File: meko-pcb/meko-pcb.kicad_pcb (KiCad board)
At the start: 4 copper layers, 37 x 69 mm, 131 parts, among them IC1 AS5600-ASOM, IC2 TPS7A2033PDBVR, IC3 TPS7A2033PDBVR, IC4 ES9218PQ, IC5 TPS7A2018PDBVR, IC6 TPS7A2033PDBVR, J1 GDEY0154D67, J2 MEM2090-00-145-00-A, J3 USB_C_Receptacle_USB2.0_16P, J4 SJ2-35954B-SMT-TR, M1 HD-EMB1204-SM, Q3 SS8050, Q4 Si1308EDL, SW1 SW_Push, SW2 SW_Push, SW3 SW_Push, SW4 SW_Push, SW5 SW_Push, SW6 SW_Push, SW7 SW_Push, U1 nRF5340-QKxx, U2 nPM1300-QEXX, Y1 ECS-2520SMV-500-GP-TR, Y2 32MHz, Y4 32.768 kHz

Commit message: many small fixes
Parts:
- removed the C24 at (40.1, 30.6)
- removed the C25 at (26.2, 33.8)
- removed the C26 at (26.2, 35.8)
- removed the C43 at (89.0, 33.3)
- removed the C45 at (94.3, 38.4)
- removed the C49 at (93.9, 40.7)
- removed the C50 at (83.9, 37.5)
- removed the C51 at (90.6, 32.9)
- removed the C52 at (90.6, 33.9)
- removed the C53 at (84.8, 36.5)
- removed the C54 at (96.4, 36.7)
- removed the C55 at (86.3, 37.3)
- removed the D2 at (74.8, 45.3)
- removed the IC5 at (22.1, 37.2)
- removed IC6: TPS7A2033PDBVR, TPS7A2018PDBVR:SOT95P280X145-5N
- removed the JP5 at (26.9, 31.0)
- removed the JP7 at (96.2, 33.3)
- removed JP9: SolderJumper_2_Open, Jumper:SolderJumper-2_P1.3mm_Open_RoundedPad1.0x1.5mm
- removed R27, R33, R35: 10k, Resistor_SMD:R_0402_1005Metric
- removed R28, R29: 47k, Resistor_SMD:R_0402_1005Metric
- removed TP13, TP16: TestPoint, TestPoint:TestPoint_Pad_D1.0mm
- removed the Y1 at (85.6, 41.4)
- added AE1: Antenna_Chip, Diode_SMD:D_1206_3216Metric, F.Cu at (127.5, 89.4)
- added C10: 100nF, Capacitor_SMD:C_0603_1608Metric, F.Cu at (25.6, 43.3)
- added C16: 10uF, Capacitor_SMD:C_0603_1608Metric, F.Cu at (22.8, 51.2)
- added C21: 10uF, Capacitor_SMD:C_0603_1608Metric, F.Cu at (22.8, 53.1)
- added C23: 10uF, Capacitor_SMD:C_0603_1608Metric, F.Cu at (22.8, 57.1)
- added C30: 1uF, Capacitor_SMD:C_0603_1608Metric, F.Cu at (22.8, 47.2)
- added C35: 1uF, Capacitor_SMD:C_0603_1608Metric, F.Cu at (22.8, 45.3)
- added C37: 1uF, Capacitor_SMD:C_0603_1608Metric, F.Cu at (31.4, 49.2)
- added C39: 1uF, Capacitor_SMD:C_0603_1608Metric, F.Cu at (31.4, 47.2)
- added C58: 2.2uF, Capacitor_SMD:C_0603_1608Metric, F.Cu at (28.5, 47.2)
- added C59: 1uF, Capacitor_SMD:C_0603_1608Metric, F.Cu at (28.5, 49.2)
- added C60: 2.2nF, Capacitor_SMD:C_0603_1608Metric, F.Cu at (28.5, 53.1)
- added C65: 4.7uF, Capacitor_SMD:C_0603_1608Metric, F.Cu at (25.6, 55.1)
- added C66: 4.7uF, Capacitor_SMD:C_0603_1608Metric, F.Cu at (25.6, 57.1)
- added C67: 12pF, Capacitor_SMD:C_0603_1608Metric, F.Cu at (22.8, 49.2)
- added C68: 12pF, Capacitor_SMD:C_0603_1608Metric, F.Cu at (31.4, 51.2)
- added C69: 1uF, Capacitor_SMD:C_0603_1608Metric, F.Cu at (25.6, 49.2)
- added C70: 4.7uF, Capacitor_SMD:C_0603_1608Metric, F.Cu at (28.5, 43.3)
- added C71: 4.7uF, Capacitor_SMD:C_0603_1608Metric, F.Cu at (28.5, 45.3)
- added C72: 1uF, Capacitor_SMD:C_0603_1608Metric, F.Cu at (25.6, 51.2)
- added C74: 4.7uF, Capacitor_SMD:C_0603_1608Metric, F.Cu at (25.6, 53.1)
- added D10: D_TVS, Diode_SMD:D_SOD-323F, F.Cu at (44.6, 52.6)
- added D11: WS2812B, LED_SMD:LED_WS2812B_PLCC4_5.0x5.0mm_P3.2mm, F.Cu at (25.4, 68.7)
- added IC1: TPS7A2033PDBVR, TPS7A2018PDBVR:SOT95P280X145-5N, F.Cu at (39.8, 53.8)
- added JP1: SolderJumper_2_Open, Jumper:SolderJumper-2_P1.3mm_Open_RoundedPad1.0x1.5mm, F.Cu at (35.0, 51.2)
- added JP2: SolderJumper_2_Open, Jumper:SolderJumper-2_P1.3mm_Open_RoundedPad1.0x1.5mm, F.Cu at (35.0, 47.6)
- added JP3: SolderJumper_2_Open, Jumper:SolderJumper-2_P1.3mm_Open_RoundedPad1.0x1.5mm, F.Cu at (35.0, 54.7)
- added L1: 10uH, Inductor_SMD:L_1008_2520Metric, F.Cu at (58.3, 44.0)
- added L2: 10uH, Inductor_SMD:L_1008_2520Metric, F.Cu at (58.3, 47.7)
- added L3: 10uH, Inductor_SMD:L_1008_2520Metric, F.Cu at (58.3, 40.2)
- added L4: 2.2uH, Inductor_SMD:L_0805_2012Metric, F.Cu at (63.0, 39.7)
- added L5: 2.2uH, Inductor_SMD:L_0805_2012Metric, F.Cu at (63.0, 42.5)
- added L6: 10uH, Inductor_SMD:L_1008_2520Metric, F.Cu at (58.3, 51.5)
- added R1: 300k, Resistor_SMD:R_0603_1608Metric, F.Cu at (41.6, 73.7)
- added R10: 47k, Resistor_SMD:R_0402_1005Metric, F.Cu at (48.1, 47.3)
- added R11: 10k, Resistor_SMD:R_0402_1005Metric, F.Cu at (48.1, 51.3)
- added R2: 47k, Resistor_SMD:R_0402_1005Metric, F.Cu at (48.1, 43.3)
- added R6: 10k, Resistor_SMD:R_0402_1005Metric, F.Cu at (48.1, 45.3)
- added R9: 47k, Resistor_SMD:R_0402_1005Metric, F.Cu at (48.1, 49.3)
- added TP1: VOUT1, TestPoint:TestPoint_Pad_D1.5mm, F.Cu at (122.9, 89.5)
- added TP2: VBAT, TestPoint:TestPoint_Pad_D1.5mm, F.Cu at (122.9, 93.0)
- added TP3: BATTHERM, TestPoint:TestPoint_Pad_D1.5mm, F.Cu at (122.9, 96.6)
- added TP4: BATGND, TestPoint:TestPoint_Pad_D1.5mm, F.Cu at (122.9, 100.1)
- added TP5: TestPoint, TestPoint:TestPoint_Pad_D1.5mm, F.Cu at (31.0, 66.9)
- added TP6: TestPoint, TestPoint:TestPoint_Pad_D1.5mm, F.Cu at (31.0, 69.9)
- added Y3: 50MGHz, Crystal:Crystal_SMD_3225-4Pin_3.2x2.5mm, F.Cu at (35.4, 69.8)
- C1: renamed from C35; footprint Capacitor_SMD:C_0402_1005Metric -> Capacitor_SMD:C_0603_1608Metric
- C11: renamed from C60; footprint Capacitor_SMD:C_0402_1005Metric -> Capacitor_SMD:C_0603_1608Metric
- C12: renamed from C68; footprint Capacitor_SMD:C_0402_1005Metric -> Capacitor_SMD:C_0603_1608Metric
- C13: renamed from C66; footprint Capacitor_SMD:C_0402_1005Metric -> Capacitor_SMD:C_0603_1608Metric
- C14: renamed from C70; footprint Capacitor_SMD:C_0402_1005Metric -> Capacitor_SMD:C_0603_1608Metric
- C15: renamed from C61; footprint Capacitor_SMD:C_0402_1005Metric -> Capacitor_SMD:C_0603_1608Metric
- C17: renamed from C67; footprint Capacitor_SMD:C_0402_1005Metric -> Capacitor_SMD:C_0603_1608Metric
- C18: renamed from C65; footprint Capacitor_SMD:C_0402_1005Metric -> Capacitor_SMD:C_0603_1608Metric
- C19: renamed from C64; footprint Capacitor_SMD:C_0402_1005Metric -> Capacitor_SMD:C_0603_1608Metric
- C2: renamed from C37; footprint Capacitor_SMD:C_0402_1005Metric -> Capacitor_SMD:C_0603_1608Metric
- C20: renamed from C69; footprint Capacitor_SMD:C_0402_1005Metric -> Capacitor_SMD:C_0603_1608Metric
- C22: renamed from C62; footprint Capacitor_SMD:C_0402_1005Metric -> Capacitor_SMD:C_0603_1608Metric
- C24: renamed from C63; footprint Capacitor_SMD:C_0402_1005Metric -> Capacitor_SMD:C_0603_1608Metric
- C25: renamed from C7; footprint Capacitor_SMD:C_0402_1005Metric -> Capacitor_SMD:C_0603_1608Metric
- C26: renamed from C23; footprint Capacitor_SMD:C_0402_1005Metric -> Capacitor_SMD:C_0603_1608Metric
- C27: value 1uF -> 10uF; footprint Capacitor_SMD:C_0402_1005Metric -> Capacitor_SMD:C_0603_1608Metric; moved to F.Cu
- C28, C34, C56: footprint Capacitor_SMD:C_0402_1005Metric -> Capacitor_SMD:C_0603_1608Metric; moved to F.Cu
- C29: renamed from C1; footprint Capacitor_SMD:C_0402_1005Metric -> Capacitor_SMD:C_0603_1608Metric
- C3: renamed from C40; footprint Capacitor_SMD:C_0402_1005Metric -> Capacitor_SMD:C_0603_1608Metric
- C31: renamed from C6; footprint Capacitor_SMD:C_0402_1005Metric -> Capacitor_SMD:C_0603_1608Metric
- C32: footprint Capacitor_SMD:C_0402_1005Metric -> Capacitor_SMD:C_0603_1608Metric
- C33: renamed from C2; footprint Capacitor_SMD:C_0402_1005Metric -> Capacitor_SMD:C_0603_1608Metric
- C36: renamed from C3; footprint Capacitor_SMD:C_0402_1005Metric -> Capacitor_SMD:C_0603_1608Metric
- C38: renamed from C4; footprint Capacitor_SMD:C_0402_1005Metric -> Capacitor_SMD:C_0603_1608Metric
- C4: renamed from C39; footprint Capacitor_SMD:C_0402_1005Metric -> Capacitor_SMD:C_0603_1608Metric
- C40: renamed from C5; footprint Capacitor_SMD:C_0402_1005Metric -> Capacitor_SMD:C_0603_1608Metric
- C41: value 1uF -> 100nF; footprint Capacitor_SMD:C_0402_1005Metric -> Capacitor_SMD:C_0603_1608Metric; moved to F.Cu
- C42: value 22uF -> 2.2nF; moved to F.Cu
- C43: renamed from C8; footprint Capacitor_SMD:C_0402_1005Metric -> Capacitor_SMD:C_0603_1608Metric
- C44: value 1uF -> 2.2nF; footprint Capacitor_SMD:C_0402_1005Metric -> Capacitor_SMD:C_0603_1608Metric; moved to F.Cu
- C45: renamed from C13; footprint Capacitor_SMD:C_0402_1005Metric -> Capacitor_SMD:C_0603_1608Metric
- C46: value 4.7uF -> 22uF; footprint Capacitor_SMD:C_0402_1005Metric -> Capacitor_SMD:C_0603_1608Metric; moved to F.Cu
- C47, C48: value 4.7uF -> 1uF; footprint Capacitor_SMD:C_0402_1005Metric -> Capacitor_SMD:C_0603_1608Metric; moved to F.Cu
- C49: renamed from C17; footprint Capacitor_SMD:C_0402_1005Metric -> Capacitor_SMD:C_0603_1608Metric
- C5: renamed from C71; footprint Capacitor_SMD:C_0402_1005Metric -> Capacitor_SMD:C_0603_1608Metric
- C50: renamed from C11; footprint Capacitor_SMD:C_0402_1005Metric -> Capacitor_SMD:C_0603_1608Metric
- C51: renamed from C18; footprint Capacitor_SMD:C_0402_1005Metric -> Capacitor_SMD:C_0603_1608Metric
- C52: renamed from C16; footprint Capacitor_SMD:C_0402_1005Metric -> Capacitor_SMD:C_0603_1608Metric
- C53: renamed from C19; footprint Capacitor_SMD:C_0402_1005Metric -> Capacitor_SMD:C_0603_1608Metric
- C54: renamed from C14; footprint Capacitor_SMD:C_0402_1005Metric -> Capacitor_SMD:C_0603_1608Metric
- C55: renamed from C20; footprint Capacitor_SMD:C_0402_1005Metric -> Capacitor_SMD:C_0603_1608Metric
- C57: renamed from C9; footprint Capacitor_SMD:C_0402_1005Metric -> Capacitor_SMD:C_0603_1608Metric
- C6: renamed from C59; footprint Capacitor_SMD:C_0402_1005Metric -> Capacitor_SMD:C_0603_1608Metric
- C61: renamed from C21; footprint Capacitor_SMD:C_0402_1005Metric -> Capacitor_SMD:C_0603_1608Metric
- C62: renamed from C12; footprint Capacitor_SMD:C_0402_1005Metric -> Capacitor_SMD:C_0603_1608Metric
- C63: renamed from C22; footprint Capacitor_SMD:C_0402_1005Metric -> Capacitor_SMD:C_0603_1608Metric
- C64: renamed from C10; footprint Capacitor_SMD:C_0402_1005Metric -> Capacitor_SMD:C_0603_1608Metric
- C7: renamed from C15; footprint Capacitor_SMD:C_0402_1005Metric -> Capacitor_SMD:C_0603_1608Metric
- C73: renamed from C30; footprint Capacitor_SMD:C_0402_1005Metric -> Capacitor_SMD:C_0603_1608Metric
- C8: renamed from C31; footprint Capacitor_SMD:C_0402_1005Metric -> Capacitor_SMD:C_0603_1608Metric
- C9: renamed from C72; footprint Capacitor_SMD:C_0402_1005Metric -> Capacitor_SMD:C_0603_1608Metric
- D6, D7: value D3V3X8U9LP3810 -> D_TVS; footprint Diodes_UDFN3810-9_TYPE_B-better-pinout:Diodes_UDFN3810-9_TYPE_B-better-pinout -> Diode_SMD:D_SOD-323F
- D9: footprint CD0201-T2.0LC:CD0201T20LC -> Diode_SMD:D_SOD-323F; moved to F.Cu
- IC3: value TPS7A2033PDBVR -> TPS7A2018PDBVR
- IC4, J4: moved to F.Cu
- TP10: renamed from TP22; value TestPoint -> DISPL_SDA; footprint TestPoint:TestPoint_Pad_D1.0mm -> TestPoint:TestPoint_Pad_D1.5mm
- TP7: renamed from TP19; value TestPoint -> SDA; footprint TestPoint:TestPoint_Pad_D1.0mm -> TestPoint:TestPoint_Pad_D1.5mm
- TP8: renamed from TP20; value TestPoint -> SCL; footprint TestPoint:TestPoint_Pad_D1.0mm -> TestPoint:TestPoint_Pad_D1.5mm
- TP9: renamed from TP21; value TestPoint -> DISPL_SCL; footprint TestPoint:TestPoint_Pad_D1.0mm -> TestPoint:TestPoint_Pad_D1.5mm
- moved C48 70.3 mm to (25.6, 47.2), turned to 0 degrees
- moved J4 69.9 mm to (41.6, 61.7), turned to 0 degrees
- moved IC4 69.4 mm to (25.0, 61.7)
- moved C56 69.0 mm to (28.5, 57.1), turned to 0 degrees
- moved C47 68.2 mm to (25.6, 45.3), turned to 0 degrees
- moved D9 67.0 mm to (44.6, 46.7), turned to 0 degrees
- moved C34 65.2 mm to (31.4, 45.3)
- moved C44 64.4 mm to (28.5, 55.1), turned to 0 degrees
- moved C28 62.3 mm to (22.8, 55.1), turned to 0 degrees
- moved C46 61.8 mm to (40.0, 68.8)
- moved C42 61.7 mm to (28.5, 51.2), turned to 0 degrees
- moved C27 59.8 mm to (22.8, 43.3), turned to 0 degrees
- moved C41 55.1 mm to (31.4, 43.3)
- moved D7 53.0 mm to (44.6, 43.8), turned to 0 degrees
- moved D6 44.4 mm to (44.6, 49.7), turned to 0 degrees
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- renumbered D13 to D1, D1 to D2, IC1 to IC5, J3 to J1, J1 to J3, JP1 to JP5, JP2 to JP6, JP3 to JP7, L1 to L7, Q3 to Q1, Q4 to Q2, R10 to R3, R11 to R4, R9 to R5, R12 to R7, R13 to R8, SW7 to SW1, SW1 to SW2, SW2 to SW3, SW3 to SW4, SW4 to SW5, SW5 to SW6, SW6 to SW7, U2 to U1, U1 to U2, Y2 to Y1, Y4 to Y2
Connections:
- net /audio/GPIO1 renamed /GPIO1
- net /audio/GPIO2 renamed /GPIO2
- C27 pad 1: REG-OUT -> +BATT
- C28 pad 1: +3V3MCLK -> REG-OUT
- C3 pad 1: (no net) -> VBUSIN
- C34 pad 1: REG-OUT -> +3V3VCCA
- C41 pad 1: GND -> /RESET
- C41 pad 2: /AUDIO_DISPL_RESETB -> GND
- C42 pad 1: /audio/PNEG -> /OUT_R
- C42 pad 2: GND -> Net-(IC4-INB_R)
- C44 pad 1: /audio/DVDD -> GND
- C44 pad 2: GND -> Net-(IC4-IN_R)
- C46 pad 1: /audio/VREF -> /PNEG
- C47 pad 1: +1V8AVCC -> /AUDIO_RESET
- C48 pad 1: +3V3AVCC -> /PNEG_VC
- C5 pad 1: VBUSOUT -> VBUS
- C73 pad 1: +3V3 -> REG-OUT
- D1 pad 1: unconnected-(D13-GND-Pad1) -> GND
- D1 pad 2: unconnected-(D13-I/O1-Pad2) -> /D+
- D1 pad 3: unconnected-(D13-I/O2-Pad3) -> /D-
- D1 pad 4: unconnected-(D13-VCC-Pad4) -> VBUS
- D6 pad 1: /DISPL_SDA -> GND
- D6 pad 2: /DISPL_SCL -> Net-(D6-A2)
- D7 pad 1: /DISPL_VCOM -> GND
- D7 pad 2: /DISPL_PREVGL -> /OUT_R
- D8 pad 2: /MEM_DAT1 -> /MEM_MISO
- D8 pad 4: /MEM_DAT0 -> unconnected-(D8-Line-6-Pad4)
- D8 pad 5: /MEM_CLK -> /MEM_SCK
- D8 pad 7: /MEM_CMD -> /MEM_MOSI
- D8 pad 8: /MEM_DAT3 -> /MEM_CS
- D8 pad 9: /MEM_DAT2 -> unconnected-(D8-Line-2-Pad9)
- D9 pad 2: Net-(D9-A2) -> /OUT_L
- IC2 pad 3: REG-OUT -> /PWR_EN3V3AVCC
- IC2 pad 5: +3V3MCLK -> +3V3AVCC
- IC3 pad 1: REG-OUT -> +3V3AVCC
- IC3 pad 3: /PWR_EN3V3AVCC -> /PWR_EN1V8AVCC
- IC3 pad 5: +3V3AVCC -> +1V8AVCC
- IC4 pad 13: /audio/PNEG -> /PNEG
- IC4 pad 14: /audio/PNEG_VC -> /PNEG_VC
- IC4 pad 15: /audio/C2 -> /C2
- IC4 pad 16: /audio/C2_VC -> /C2_VC
- IC4 pad 17: /audio/C1_VC -> /C1_VC
- IC4 pad 18: /audio/C1 -> /C1
- IC4 pad 2: unconnected-(IC4-XO-Pad2) -> /XO
- IC4 pad 22: /audio/OUT_L -> /OUT_L
- IC4 pad 27: /audio/AVCC_DAC -> /AVCC_DAC
- IC4 pad 28: /audio/VREF -> /VREF
- IC4 pad 3: /audio/XI -> /XI
- IC4 pad 31: /audio/DVDD -> /DVDD
- IC4 pad 36: /AUDIO_DATA_CLK/BOOT -> /AUDIO_DATA_CLK
- IC4 pad 37: /AUDIO_DISPL_RESETB -> /AUDIO_RESET
- IC4 pad 9: /audio/OUT_R -> /OUT_R
- J2 pad 1: /MEM_DAT2 -> unconnected-(J2-DAT2-Pad1)
- J2 pad 2: /MEM_DAT3 -> /MEM_CS
- J2 pad 3: /MEM_CMD -> /MEM_MOSI
- J2 pad 5: /MEM_CLK -> /MEM_SCK
- J2 pad 7: /MEM_DAT0 -> /MEM_MISO
- J2 pad 8: /MEM_DAT1 -> unconnected-(J2-DAT1-Pad8)
- J3 pad 10: /AUDIO_DISPL_RESETB -> /DISPL_RESET
- J4 pad R1: /audio/OUT_R -> /OUT_R
- J4 pad S: Net-(D9-A2) -> Net-(D6-A2)
- J4 pad T: /audio/OUT_L -> /OUT_L
- SW7 pad 2: /ESP_EN -> /RESET
- U1 pad 10: unconnected-(U2-GPIO3-Pad10) -> /PMIC_GPIO3
- U1 pad 11: unconnected-(U2-GPIO4-Pad11) -> /PMIC_GPIO5
- U1 pad 12: unconnected-(U2-VDDIO-Pad12) -> +3V3
- U1 pad 20: unconnected-(U2-VSYS-Pad20) -> REG-OUT
- U1 pad 22: VBUSOUT -> VBUS
- U1 pad 4: unconnected-(U2-PVDD-Pad4) -> REG-OUT
- U1 pad 7: unconnected-(U2-GPIO0-Pad7) -> /PMIC_GPIO0
- U1 pad 8: unconnected-(U2-GPIO1-Pad8) -> /PMIC_GPIO1
- U1 pad 9: unconnected-(U2-GPIO2-Pad9) -> /PMIC_GPIO2
- U2 pad A17: unconnected-(U1-P1.13-PadA17) -> /DISPL_RESET
- U2 pad A5: VBUSOUT -> VBUS
- U2 pad AC31: unconnected-(U1-~{RESET}-PadAC31) -> /RESET
- U2 pad AE1: unconnected-(U1-TWI/P1.02-PadAE1) -> /BTN_VOL_UP
- U2 pad AE31: unconnected-(U1-AIN7/P0.28-PadAE31) -> /PMIC_GPIO3
- U2 pad AF2: unconnected-(U1-TWI/P1.03-PadAF2) -> /I2C_SCL
- U2 pad AH2: unconnected-(U1-SCK/TRACEDATA3/P0.08-PadAH2) -> /MEM_SCK
- U2 pad AJ1: unconnected-(U1-MOSI/TRACEDATA2/P0.09-PadAJ1) -> /MEM_MOSI
- U2 pad AK16: unconnected-(U1-P0.20-PadAK16) -> /AUDIO_DATA_CLK
- U2 pad AK18: unconnected-(U1-P0.22-PadAK18) -> /LED
- U2 pad AK2: unconnected-(U1-MISO/TRACEDATA1/P0.10-PadAK2) -> /MEM_MISO
- U2 pad AK20: unconnected-(U1-P0.23-PadAK20) -> /BTN_SIDE_R
- U2 pad AK22: unconnected-(U1-P1.05-PadAK22) -> /BTN_VOL_DWN
- U2 pad AK24: unconnected-(U1-P1.07-PadAK24) -> /MEM_COM
- U2 pad AK26: unconnected-(U1-P1.09-PadAK26) -> /PWR_EN3V3AVCC
- U2 pad AK28: unconnected-(U1-AIN4/P0.25-PadAK28) -> /PMIC_GPIO0
- U2 pad AK30: unconnected-(U1-AIN6/P0.27-PadAK30) -> /PMIC_GPIO2
- U2 pad AK4: unconnected-(U1-CSN/TRACEDATA0/P0.11-PadAK4) -> /MEM_CS
- U2 pad AL13: unconnected-(U1-P0.19-PadAL13) -> /AUDIO_DATA_2
- U2 pad AL15: unconnected-(U1-P0.21-PadAL15) -> /AUDIO_DATA1
- U2 pad AL19: unconnected-(U1-P1.04-PadAL19) -> /I2C_SDA
- U2 pad AL21: unconnected-(U1-P1.06-PadAL21) -> /DISPL_BUSY
- U2 pad AL23: unconnected-(U1-P1.08-PadAL23) -> /PWR_EN1V8AVCC
- U2 pad AL27: unconnected-(U1-P0.24-PadAL27) -> /BTN_SIDE_L
- U2 pad AL29: unconnected-(U1-AIN5/P0.26-PadAL29) -> /PMIC_GPIO1
- U2 pad B14: unconnected-(U1-P1.15-PadB14) -> /DISPL_~{D/C}
- U2 pad B16: unconnected-(U1-P1.14-PadB16) -> /DISPL_~{CS}
- U2 pad B18: unconnected-(U1-P1.12-PadB18) -> /PWR_EN3V3VCCA
- U2 pad B20: unconnected-(U1-P1.11-PadB20) -> /HAPTIC_MOTOR
- U2 pad B22: unconnected-(U1-P0.31-PadB22) -> /DISPL_SDA
- U2 pad B24: unconnected-(U1-P0.30-PadB24) -> /DISPL_SCL
- U2 pad M2: unconnected-(U1-P1.00-PadM2) -> /BTN_PWR
- U2 pad P2: unconnected-(U1-P1.01-PadP2) -> /AUDIO_RESET
- U2 pad R31: unconnected-(U1-P1.10-PadR31) -> /AUDIO_TN
- U2 pad U31: unconnected-(U1-P0.29-PadU31) -> /PMIC_GPIO5
- U2 pad V2: unconnected-(U1-AIN0/P0.04-PadV2) -> /HAL_OUT
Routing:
- net REG-OUT: vias 12 -> 0
- net GND: vias 540 -> 0
- net /PWR_EN3V3VCCA: vias 3 -> 0
- net /PWR_EN3V3AVCC: vias 2 -> 0
- net /PWR_EN1V8AVCC: vias 2 -> 0
- net /MEM_DAT3: vias 2 -> 0
- net /MEM_DAT2: vias 2 -> 0
- net /MEM_COM: vias 2 -> 0
- net /MEM_CMD: vias 2 -> 0
- net /LED: vias 3 -> 0
- net /I2C_SDA: vias 5 -> 0
- net /I2C_SCL: vias 5 -> 0
- net /HAPTIC_MOTOR: vias 4 -> 0
- net /HAL_OUT: vias 1 -> 0
- net /ESP_EN: vias 2 -> 0
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
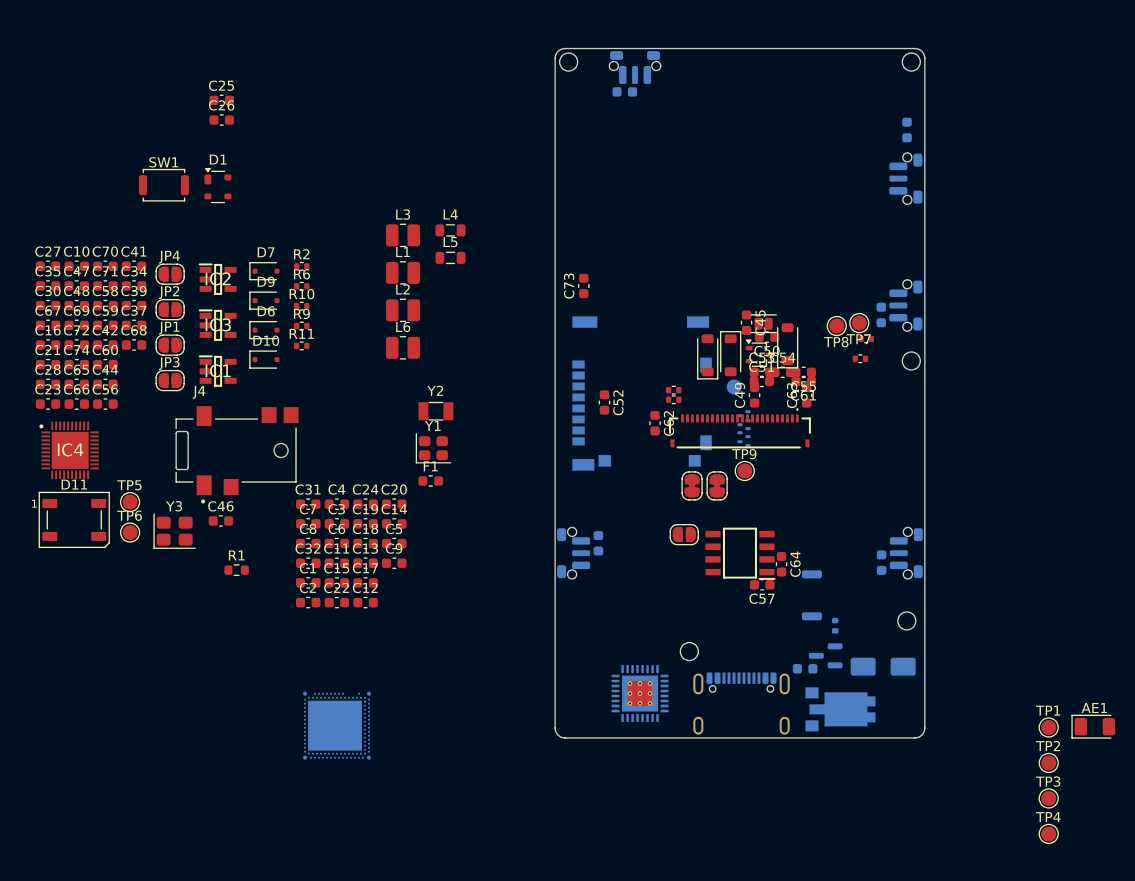
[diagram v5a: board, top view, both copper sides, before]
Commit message: switched from the ESS dac to a TI dac
the preformance is better/same, its easier to implement, cheaper, in stock at lcsc
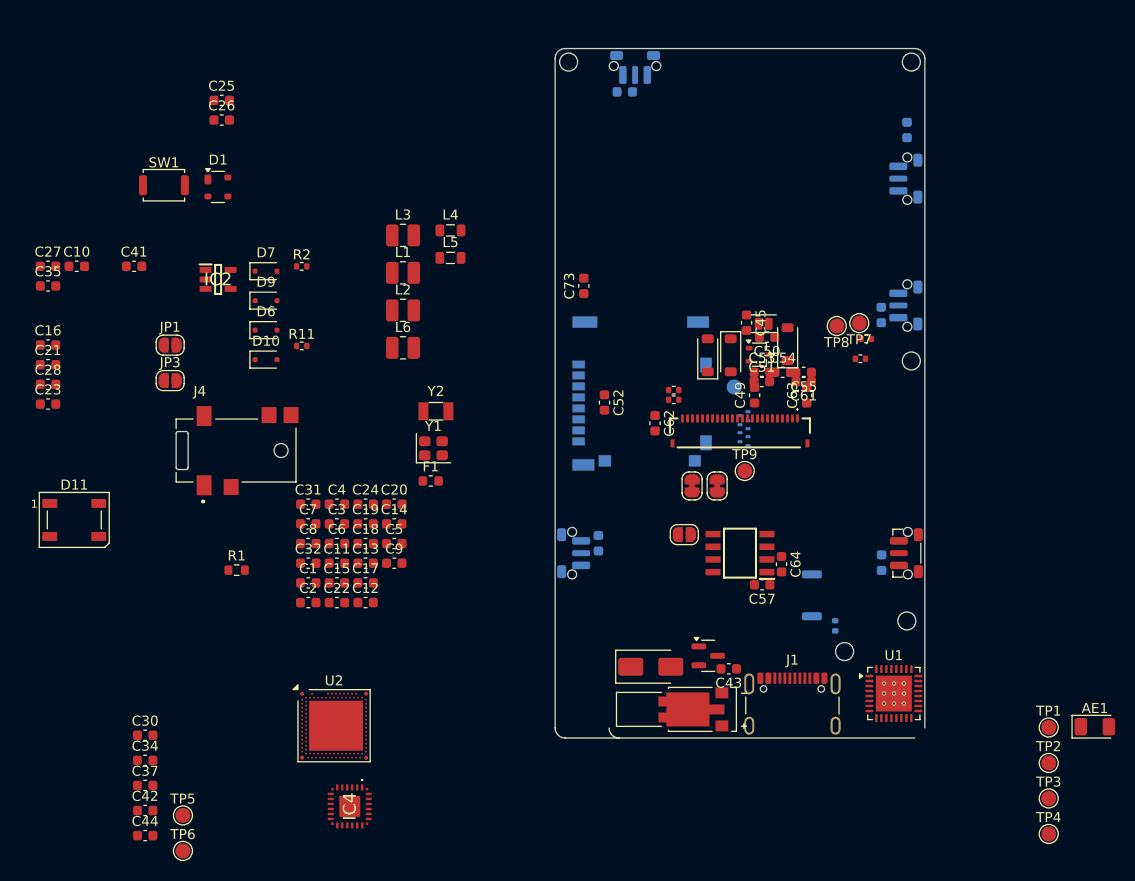
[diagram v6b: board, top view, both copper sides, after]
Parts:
- removed C39, C47, C48, C59, C69, C72: 1uF, Capacitor_SMD:C_0603_1608Metric
- removed C46: 22uF, Capacitor_SMD:C_0603_1608Metric
- removed C56, C60: 2.2nF, Capacitor_SMD:C_0603_1608Metric
- removed C58: 2.2uF, Capacitor_SMD:C_0603_1608Metric
- removed C65, C66, C70, C71, C74: 4.7uF, Capacitor_SMD:C_0603_1608Metric
- removed C67, C68: 12pF, Capacitor_SMD:C_0603_1608Metric
- removed IC1: TPS7A2033PDBVR, TPS7A2018PDBVR:SOT95P280X145-5N
- removed IC3: TPS7A2018PDBVR, TPS7A2018PDBVR:SOT95P280X145-5N
- removed JP2, JP4: SolderJumper_2_Open, Jumper:SolderJumper-2_P1.3mm_Open_RoundedPad1.0x1.5mm
- removed R10, R9: 47k, Resistor_SMD:R_0402_1005Metric
- removed R6: 10k, Resistor_SMD:R_0402_1005Metric
- removed Y3: 50MGHz, Crystal:Crystal_SMD_3225-4Pin_3.2x2.5mm
- C42, C44: value 2.2nF -> 1uF
- C43, D2, J1, M1, Q1, SW6, U1, U2: moved to F.Cu
- H3: moved to B.Cu
- IC4: value ES9218PQ -> TAD5212IRGER; footprint ES9218PQ:QFN40P500X500X80-41N-D -> TAD5112IRGER:TAD5112IRGER
- TP5: value TestPoint -> DISPL_SCL
- TP6: value TestPoint -> DISPL_SDA
- moved C34 47.5 mm to (32.5, 92.7)
- moved C42 46.8 mm to (32.5, 97.8)
- moved C37 46.1 mm to (32.5, 95.3)
- moved C44 45.3 mm to (32.5, 100.3)
- moved IC4 45.3 mm to (52.9, 97.4), turned to -90 degrees
- moved C30 44.1 mm to (32.5, 90.2)
- moved TP6 32.3 mm to (36.2, 101.8)
- moved TP5 31.8 mm to (36.2, 98.3)
- moved U1 25.4 mm to (107.4, 86.1), turned to 0 degrees
- moved D2 23.3 mm to (83.1, 83.4), turned to 0 degrees
- moved H3 15.5 mm to (102.5, 81.9), turned to 180 degrees
- moved M1 12.9 mm to (88.2, 87.6), turned to 180 degrees
- moved Q1 11.8 mm to (88.8, 82.3), turned to 0 degrees
- moved C43 7.64 mm to (90.9, 83.6), turned to 180 degrees
- moved J1 5.09 mm to (97.2, 88.2), turned to 0 degrees
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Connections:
- C30 pad 1: REG-OUT -> +3V3AVDD
- C34 pad 1: +3V3VCCA -> GND
- C34 pad 2: GND -> Net-(IC4-DREG)
- C35 pad 1: +3V3AVCC -> +3V3AVDD
- C37 pad 1: +3V3AVCC -> Net-(IC4-VREF)
- C42 pad 1: /OUT_R -> Net-(IC4-MICBIAS)
- C42 pad 2: Net-(IC4-INB_R) -> GND
- C44 pad 2: Net-(IC4-IN_R) -> +3V3
- IC2 pad 5: +3V3AVCC -> +3V3AVDD
- IC4 pad 1: GND -> Net-(IC4-DREG)
- IC4 pad 10: GND -> /AUDIO_GPIO2
- IC4 pad 11: GND -> /AUDIO_GPO1
- IC4 pad 12: GND -> /AUDIO_GPI1
- IC4 pad 13: /PNEG -> /AUDIO_ADDR
- IC4 pad 14: /PNEG_VC -> Net-(IC4-MICBIAS)
- IC4 pad 15: /C2 -> GND
- IC4 pad 16: /C2_VC -> GND
- IC4 pad 17: /C1_VC -> GND
- IC4 pad 18: /C1 -> GND
- IC4 pad 19: +1V8AVCC -> unconnected-(IC4-OUT1M-Pad19)
- IC4 pad 2: /XO -> /BCLK
- IC4 pad 20: +3V3AVCC -> unconnected-(IC4-OUT1P-Pad20)
- IC4 pad 21: GND -> unconnected-(IC4-OUT2P-Pad21)
- IC4 pad 22: /OUT_L -> unconnected-(IC4-OUT2M-Pad22)
- IC4 pad 23: Net-(IC4-IN_L) -> +3V3AVDD
- IC4 pad 24: Net-(IC4-INB_L) -> Net-(IC4-VREF)
- IC4 pad 25: unconnected-(IC4-AUX_L-Pad25) -> GND
- IC4 pad 27: /AVCC_DAC -> GND
- IC4 pad 28: /VREF -> GND
- IC4 pad 29: +3V3 -> GND
- IC4 pad 3: /XI -> /FSYNC
- IC4 pad 4: +3V3VCCA -> /DOUT
- IC4 pad 5: GND -> /DIN
- IC4 pad 6: unconnected-(IC4-AUX_R-Pad6) -> +3V3
- IC4 pad 7: Net-(IC4-INB_R) -> /I2C_SCL
- IC4 pad 8: Net-(IC4-IN_R) -> /I2C_SDA
- IC4 pad 9: /OUT_R -> /AUDIO_GPIO1
- TP5 pad 1: +3V3VCCA -> /SWDIO
- TP6 pad 1: +1V8AVCC -> /SWDIO
- U2 pad A17: /DISPL_RESET -> /DISPL_~{CS}
- U2 pad AA31: unconnected-(U2-SWDIO-PadAA31) -> /SWDIO
- U2 pad AE31: /PMIC_GPIO3 -> /AUDIO_GPO1
- U2 pad AK10: unconnected-(U2-IO2/P0.15-PadAK10) -> /PMIC_GPIO0
- U2 pad AK12: unconnected-(U2-SCK/P0.17-PadAK12) -> /PMIC_GPIO2
- U2 pad AK14: unconnected-(U2-CSN/P0.18-PadAK14) -> /PMIC_GPIO3
- U2 pad AK16: /AUDIO_DATA_CLK -> /DISPL_SCL
- U2 pad AK18: /LED -> /BCLK
- U2 pad AK20: /BTN_SIDE_R -> /FSYNC
- U2 pad AK28: /PMIC_GPIO0 -> /DIN
- U2 pad AK30: /PMIC_GPIO2 -> /AUDIO_GPIO2
- U2 pad AK6: unconnected-(U2-DCX/TRACECLK/P0.12-PadAK6) -> /LED
- U2 pad AK8: unconnected-(U2-IO1/P0.14-PadAK8) -> /BTN_SIDE_L
- U2 pad AL13: /AUDIO_DATA_2 -> /PMIC_GPIO5
- U2 pad AL15: /AUDIO_DATA1 -> /DISPL_SDA
- U2 pad AL23: /PWR_EN1V8AVCC -> unconnected-(U2-P1.08-PadAL23)
- U2 pad AL27: /BTN_SIDE_L -> /DOUT
- U2 pad AL29: /PMIC_GPIO1 -> /AUDIO_GPIO1
- U2 pad AL5: unconnected-(U2-IO0/P0.13-PadAL5) -> /BTN_SIDE_R
- U2 pad AL9: unconnected-(U2-IO3/P0.16-PadAL9) -> /PMIC_GPIO1
- U2 pad B14: /DISPL_~{D/C} -> /HAPTIC_MOTOR
- U2 pad B16: /DISPL_~{CS} -> /DISPL_~{D/C}
- U2 pad B18: /PWR_EN3V3VCCA -> /DISPL_RESET
- U2 pad B20: /HAPTIC_MOTOR -> unconnected-(U2-P1.11-PadB20)
- U2 pad B22: /DISPL_SDA -> unconnected-(U2-P0.31-PadB22)
- U2 pad B24: /DISPL_SCL -> /AUDIO_ADDR
- U2 pad U31: /PMIC_GPIO5 -> /AUDIO_GPI1
- U2 pad W31: unconnected-(U2-SWDCLK-PadW31) -> /SWDIO
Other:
- outline, holes or cut-outs redrawn

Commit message: added final touches
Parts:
- removed C73: 100nF, Capacitor_SMD:C_0603_1608Metric
- removed F1: 500mA, Fuse:Fuse_0603_1608Metric
- added CN2: ~, PJ-242:AUDIO-SMD_PJ-342, F.Cu at (90.6, 29.8)
- added D12: D_TVS, Diode_SMD:D_SOD-323F, F.Cu at (63.7, 51.7)
- added D14: D_TVS, Diode_SMD:D_SOD-323F, F.Cu at (63.7, 54.6)
- added D15: white, LED_SMD:LED_0603_1608Metric, F.Cu at (40.6, 77.1)
- added D16: blue, LED_SMD:LED_0603_1608Metric, F.Cu at (40.6, 79.7)
- added R10: 10k, Resistor_SMD:R_0402_1005Metric, F.Cu at (62.4, 66.7)
- added R12: 10k, Resistor_SMD:R_0402_1005Metric, F.Cu at (65.3, 60.7)
- added R13: 10k, Resistor_SMD:R_0402_1005Metric, F.Cu at (65.3, 62.7)
- added R14: 10k, Resistor_SMD:R_0402_1005Metric, F.Cu at (65.3, 64.7)
- added R15: 10k, Resistor_SMD:R_0402_1005Metric, F.Cu at (65.3, 66.7)
- added R6: 10k, Resistor_SMD:R_0402_1005Metric, F.Cu at (59.5, 68.6)
- added R9: 10k, Resistor_SMD:R_0402_1005Metric, F.Cu at (62.4, 64.7)
- added TP11: DISPL_SCL, TestPoint:TestPoint_Pad_D1.0mm, F.Cu at (48.3, 54.4)
- added TP12: DISPL_SDA, TestPoint:TestPoint_Pad_D1.0mm, F.Cu at (48.3, 57.9)
- added TP13: DISPL_SCL, TestPoint:TestPoint_Pad_D1.0mm, F.Cu at (51.9, 40.2)
- added TP14: DISPL_SDA, TestPoint:TestPoint_Pad_D1.0mm, F.Cu at (51.9, 43.7)
- added TP15: DISPL_SCL, TestPoint:TestPoint_Pad_D1.0mm, F.Cu at (51.9, 47.3)
- added TP16: DISPL_SDA, TestPoint:TestPoint_Pad_D1.0mm, F.Cu at (51.9, 50.8)
- added TP17: DISPL_SDA, TestPoint:TestPoint_Pad_D1.0mm, F.Cu at (51.9, 54.4)
- added TP18: DISPL_SDA, TestPoint:TestPoint_Pad_D1.0mm, F.Cu at (51.9, 57.9)
- added TP19: DISPL_SDA, TestPoint:TestPoint_Pad_D1.0mm, F.Cu at (55.4, 40.2)
- added TP20: DISPL_SDA, TestPoint:TestPoint_Pad_D1.0mm, F.Cu at (55.4, 43.7)
- added TP21: DISPL_SDA, TestPoint:TestPoint_Pad_D1.0mm, F.Cu at (55.4, 47.3)
- C29, C33, C36, C38, C40, D8, J2, R5, SW2, SW3, SW4, SW5, SW7: moved to F.Cu
- D11: value WS2812B -> Orange; footprint LED_SMD:LED_WS2812B_PLCC4_5.0x5.0mm_P3.2mm -> LED_SMD:LED_0603_1608Metric
- J4: value SJ2-35954B-SMT-TR -> Conn_ARM_SWD_TagConnect_TC2030-NL; footprint SJ2-35954B-SMT-TR:CUI_SJ2-35954B-SMT-TR -> Connector:Tag-Connect_TC2030-IDC-NL_2x03_P1.27mm_Vertical
- TP1, TP2, TP3, TP4, TP5, TP6, TP7, TP8, TP9: footprint TestPoint:TestPoint_Pad_D1.5mm -> TestPoint:TestPoint_Pad_D1.0mm
- TP10: footprint TestPoint:TestPoint_Pad_D1.5mm -> TestPoint:TestPoint_Pad_D1.0mm; moved to F.Cu
- moved AE1 102.2 mm to (25.8, 79.8)
- moved TP4 92.4 mm to (44.8, 50.8)
- moved TP1 92.4 mm to (44.8, 40.2)
- moved TP2 92.4 mm to (44.8, 43.7)
- moved TP3 92.4 mm to (44.8, 47.3)
- moved U1 74.8 mm to (34.5, 69.6)
- moved C57 62.6 mm to (41.0, 42.2), turned to 0 degrees
- moved C54 60.3 mm to (37.0, 64.7)
- moved C55 59.1 mm to (41.0, 39.6), turned to 0 degrees
- moved C64 59.0 mm to (41.0, 52.2), turned to 0 degrees
- moved C61 58.3 mm to (41.0, 44.7), turned to 0 degrees
- moved C63 58.0 mm to (41.0, 49.7), turned to 0 degrees
- moved C50 57.9 mm to (37.0, 54.7), turned to 0 degrees
- moved C53 57.8 mm to (37.0, 62.2)
- moved C51 57.2 mm to (37.0, 57.2)
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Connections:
- D1 pad 4: VBUS -> VBUSIN
- D10 pad 2: /AUDIO_TN -> Net-(D10-A2)
- D11 pad 1: REG-OUT -> Net-(D11-K)
- D11 pad 2: unconnected-(D11-DOUT-Pad2) -> Net-(D11-A)
- D6 pad 2: Net-(D6-A2) -> /AUDIO_TN
- D7 pad 2: /OUT_R -> Net-(D7-A2)
- D9 pad 2: /OUT_L -> Net-(D9-A2)
- IC4 pad 19: unconnected-(IC4-OUT1M-Pad19) -> /OUT_R
- IC4 pad 20: unconnected-(IC4-OUT1P-Pad20) -> /OUT_L
- IC4 pad 21: unconnected-(IC4-OUT2P-Pad21) -> Net-(D9-A2)
- IC4 pad 22: unconnected-(IC4-OUT2M-Pad22) -> Net-(D7-A2)
- J1 pad A4: Net-(F1-Pad2) -> VBUSIN
- J1 pad A9: Net-(F1-Pad2) -> VBUSIN
- J1 pad B4: Net-(F1-Pad2) -> VBUSIN
- J1 pad B9: Net-(F1-Pad2) -> VBUSIN
- JP1 pad 1: /RESET -> /PMIC_GPIO0
- JP1 pad 2: /PMIC_GPIO0 -> /RESET
- TP5 pad 1: /SWDIO -> /LSIN2
- TP6 pad 1: /SWDIO -> /LSOUT2
- U1 pad 25: unconnected-(U1-LED0-Pad25) -> Net-(D11-K)
- U1 pad 26: unconnected-(U1-LED1-Pad26) -> Net-(D16-K)
- U1 pad 27: unconnected-(U1-LED2-Pad27) -> Net-(D15-K)
- U1 pad 30: unconnected-(U1-LSIN2/VINLDO2-Pad30) -> /LSIN2
- U1 pad 31: unconnected-(U1-LSOUT2/VOUTLDO2-Pad31) -> /LSOUT2
- U2 pad AA1: unconnected-(U2-NFC2/P0.03-PadAA1) -> Net-(U2-NFC2/P0.03)
- U2 pad AB2: unconnected-(U2-AIN2/P0.06-PadAB2) -> Net-(U2-AIN2/P0.06)
- U2 pad AD2: unconnected-(U2-AIN3/P0.07-PadAD2) -> Net-(U2-AIN3/P0.07)
- U2 pad AL23: unconnected-(U2-P1.08-PadAL23) -> Net-(U2-P1.08)
- U2 pad B20: unconnected-(U2-P1.11-PadB20) -> Net-(U2-P1.11)
- U2 pad B22: unconnected-(U2-P0.31-PadB22) -> Net-(U2-P0.31)
- U2 pad P2: /AUDIO_RESET -> Net-(U2-P1.01)
- U2 pad W1: unconnected-(U2-NFC1/P0.02-PadW1) -> Net-(U2-NFC1/P0.02)
- U2 pad W31: /SWDIO -> /SWDCLK
- U2 pad Y2: unconnected-(U2-AIN1/P0.05-PadY2) -> Net-(U2-AIN1/P0.05)
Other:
- outline, holes or cut-outs redrawn

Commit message: Smalll updatesd
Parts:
- removed JP1: SolderJumper_2_Open, Jumper:SolderJumper-2_P1.3mm_Open_RoundedPad1.0x1.5mm
- removed JP5, JP6: SolderJumper_2_Bridged, Jumper:SolderJumper-2_P1.3mm_Bridged_RoundedPad1.0x1.5mm
- removed TP19, TP21: DISPL_SDA, TestPoint:TestPoint_Pad_D1.0mm
- added SW8: SW_Push, Button_Switch_SMD:SW_Push_SPST_NO_Alps_SKRK, F.Cu at (41.3, 61.9)
- R13, R14, R15: value 10k -> 220R
- moved H3 20.5 mm to (82.1, 83.8)
- moved CN2 8.87 mm to (99.5, 29.8)
- moved Q1 6.07 mm to (77.9, 79.8)
- moved C43 1.78 mm to (85.0, 81.9), turned to -90 degrees
- moved J1 1.19 mm to (92.0, 88.2)
- moved C29 1.00 mm to (81.5, 25.8)
- moved SW2 1.00 mm to (82.5, 23.2)
- moved D2 0.18 mm to (77.5, 83.4)
- moved U2 0.10 mm to (48.0, 64.6), turned to 180 degrees
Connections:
- U2 pad AE1: /BTN_VOL_UP -> /I2C_SDA
- U2 pad AL19: /I2C_SDA -> /DISPL_~{D/C}
- U2 pad AL23: Net-(U2-P1.08) -> /DISPL_~{CS}
- U2 pad M2: /BTN_PWR -> /BTN_VOL_UP
- U2 pad P2: Net-(U2-P1.01) -> /BTN_PWR
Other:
- outline, holes or cut-outs redrawn
